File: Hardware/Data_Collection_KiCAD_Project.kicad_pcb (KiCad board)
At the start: 4 copper layers, 80 x 93.3 mm, 78 parts, among them J1 L717SDC37P1ACH4F, J2 Conn_Coaxial, J3 10118192-0001LF, Q1 SI1040X-T1-GE3, SW1 MCU Reset, U1 BNO055, U2 W25Q32JVSS, U3 MAX-8Q, U4 LP38692MPX-ADJ, U5 USBLC6-2SC6, U6 MCP9808_MSOP, U7 MS5607-02BA, U8 KX134-1211, U9 STM32L562VET6Q, Y1 32.768kHz, Y2 32MHz

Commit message: wtf is wrong with my github install
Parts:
- removed the G*** at (102.6, 98.5)
- JP1: footprint Jumper:SolderJumper-2_P1.3mm_Bridged_Pad1.0x1.5mm -> Jumper:SolderJumper-2_P1.3mm_Open_Pad1.0x1.5mm
- moved C30 69.1 mm to (130.7, 84.2), turned to 45 degrees
- moved U8 65.9 mm to (102.0, 133.0)
- moved C13 65.9 mm to (100.0, 135.9)
- moved C28 65.9 mm to (104.0, 135.9)
- moved U2 63.3 mm to (130.5, 90.2), turned to 45 degrees
- moved C27 60.1 mm to (104.4, 119.2)
- moved C1 60.1 mm to (104.2, 122.9)
- moved U1 60.1 mm to (109.1, 122.3)
- moved Y1 60.1 mm to (108.0, 116.3)
- moved C3 60.1 mm to (109.7, 113.5)
- moved C4 60.1 mm to (106.3, 113.5)
- moved C12 40.0 mm to (129.4, 101.5)
- moved U7 40.0 mm to (129.4, 105.1)
- moved C8 19.2 mm to (144.1, 104.9), turned to 90 degrees
- moved C7 19.1 mm to (142.6, 104.9), turned to 90 degrees
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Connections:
- D2 pad 2: Net-(D2-Pad2) -> unconnected-(D2-Pad2)
- D3 pad 2: Net-(D3-Pad2) -> unconnected-(D3-Pad2)
- D4 pad 2: Net-(D4-Pad2) -> unconnected-(D4-Pad2)
- D5 pad 2: Net-(D5-Pad2) -> unconnected-(D5-Pad2)
- D6 pad 2: Net-(D6-Pad2) -> unconnected-(D6-Pad2)
- U4 pad 1: GND -> +5V
- U4 pad 2: +5V -> Net-(R4-Pad1)
- U4 pad 3: +5V -> +3V3
- U4 pad 4: Net-(R4-Pad1) -> +5V
- U4 pad 5: +3V3 -> GND
- U9 pad 29: /FLASH_CLK -> /TELEMETRY_SCK
- U9 pad 30: /FLASH_MISO -> /TELEMETRY_MISO
- U9 pad 31: /FLASH_MOSI -> /TELEMETRY_MOSI
- U9 pad 35: Net-(D2-Pad2) -> unconnected-(U9-Pad35)
- U9 pad 36: Net-(D3-Pad2) -> unconnected-(U9-Pad36)
- U9 pad 37: Net-(D4-Pad2) -> /ABORT_1
- U9 pad 38: Net-(D5-Pad2) -> /ABORT_2
- U9 pad 39: Net-(D6-Pad2) -> unconnected-(U9-Pad39)
- U9 pad 52: /TELEMETRY_SCK -> /FLASH_CLK
- U9 pad 53: /TELEMETRY_MISO -> /FLASH_MISO
- U9 pad 54: /TELEMETRY_MOSI -> /FLASH_MOSI
- U9 pad 61: /ABORT_2 -> unconnected-(U9-Pad61)
- U9 pad 62: /ABORT_1 -> unconnected-(U9-Pad62)
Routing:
- net /SWCLK: track 0.00 -> 48.6 mm, vias 0 -> 2
- net /SWDIO: track 0.00 -> 42.5 mm, vias 0 -> 1
- net /GPS_TX: track 0.00 -> 39.9 mm, vias 0 -> 2
- net /GPS_RX: track 0.00 -> 38.7 mm
- net /~{GPS_RESET}: track 0.00 -> 35.6 mm
- net /ABORT_2: track 0.00 -> 32.3 mm, vias 0 -> 1
- net /ALERT_SDA: track 0.00 -> 31.5 mm
- net /ALERT_SCL: track 0.00 -> 30.2 mm
- net /ALERT_EN: track 0.00 -> 29.1 mm, vias 0 -> 1
- net /TELEMETRY_MOSI: track 0.00 -> 29.0 mm, vias 0 -> 2
- net /ABORT_1: track 0.00 -> 29.0 mm, vias 0 -> 1
- net /TELEMETRY_SCK: track 0.00 -> 27.2 mm, vias 0 -> 2
- net /TELEMETRY_MISO: track 0.00 -> 23.0 mm
- net /SENSOR_SCL: track 0.00 -> 20.9 mm
- net /SENSOR_SDA: track 0.00 -> 20.3 mm
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
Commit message: almost there
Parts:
- moved C2 106.7 mm to (112.3, 117.8)
- moved TP1 93.8 mm to (111.1, 121.2)
- moved TP3 89.8 mm to (122.7, 128.7)
- moved TP2 89.5 mm to (117.5, 110.3)
- moved C29 63.7 mm to (106.1, 131.4), turned to 180 degrees
- moved U6 57.6 mm to (108.2, 135.4), turned to 90 degrees
- moved R12 57.1 mm to (135.8, 95.5), turned to 180 degrees
- moved R11 53.9 mm to (139.3, 95.5)
- moved D6 47.3 mm to (154.0, 99.8), turned to -90 degrees
- moved R10 46.6 mm to (152.1, 99.7), turned to 90 degrees
- moved D4 44.4 mm to (154.0, 91.2), turned to -90 degrees
- moved C33 44.1 mm to (175.2, 114.0)
- moved R7 43.8 mm to (152.1, 87.0), turned to 90 degrees
- moved R9 39.7 mm to (152.1, 95.5), turned to 90 degrees
- moved D5 39.7 mm to (154.0, 95.5), turned to -90 degrees
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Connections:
- D2 pad 1: Net-(D2-Pad1) -> GND
- D2 pad 2: unconnected-(D2-Pad2) -> Net-(D2-Pad2)
- D3 pad 1: Net-(D3-Pad1) -> GND
- D3 pad 2: unconnected-(D3-Pad2) -> Net-(D3-Pad2)
- D4 pad 1: Net-(D4-Pad1) -> GND
- D4 pad 2: unconnected-(D4-Pad2) -> Net-(D4-Pad2)
- D5 pad 1: Net-(D5-Pad1) -> GND
- D5 pad 2: unconnected-(D5-Pad2) -> Net-(D5-Pad2)
- D6 pad 1: Net-(D6-Pad1) -> GND
- D6 pad 2: unconnected-(D6-Pad2) -> Net-(D6-Pad2)
- R10 pad 1: GND -> Net-(D6-Pad2)
- R10 pad 2: Net-(D6-Pad1) -> unconnected-(R10-Pad2)
- R6 pad 1: GND -> Net-(D2-Pad2)
- R6 pad 2: Net-(D2-Pad1) -> unconnected-(R6-Pad2)
- R7 pad 1: GND -> Net-(D3-Pad2)
- R7 pad 2: Net-(D3-Pad1) -> unconnected-(R7-Pad2)
- R8 pad 1: GND -> Net-(D4-Pad2)
- R8 pad 2: Net-(D4-Pad1) -> unconnected-(R8-Pad2)
- R9 pad 1: GND -> Net-(D5-Pad2)
- R9 pad 2: Net-(D5-Pad1) -> unconnected-(R9-Pad2)
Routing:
- net /SENSOR_SCL: track 20.9 -> 126.4 mm, vias 0 -> 6
- net /SENSOR_SDA: track 20.3 -> 114.4 mm
- net (no net): track 10.6 -> 0.00 mm, vias 6 -> 1
- net /BNO055/~{BNO055_BTL}: track 0.00 -> 6.62 mm
- net /KX134-1211/KX134_INT1: track 0.00 -> 5.42 mm
- net /BNO055/~{BNO055_RESET}: track 0.00 -> 4.76 mm
- net +3V3: track 90.2 -> 92.8 mm, vias 24 -> 26
- net /~{GPS_RESET}: track 35.6 -> 37.8 mm
- net Net-(D2-Pad2): track 0.00 -> 1.98 mm
- net Net-(D3-Pad2): track 0.00 -> 1.96 mm
- net Net-(D4-Pad2): track 0.00 -> 1.94 mm
- net Net-(D6-Pad2): track 0.00 -> 1.92 mm
- net Net-(D5-Pad2): track 0.00 -> 1.91 mm
- net GND: track 132.6 -> 134.4 mm, vias 70 -> 71
- net Net-(C2-Pad2): track 0.00 -> 1.62 mm

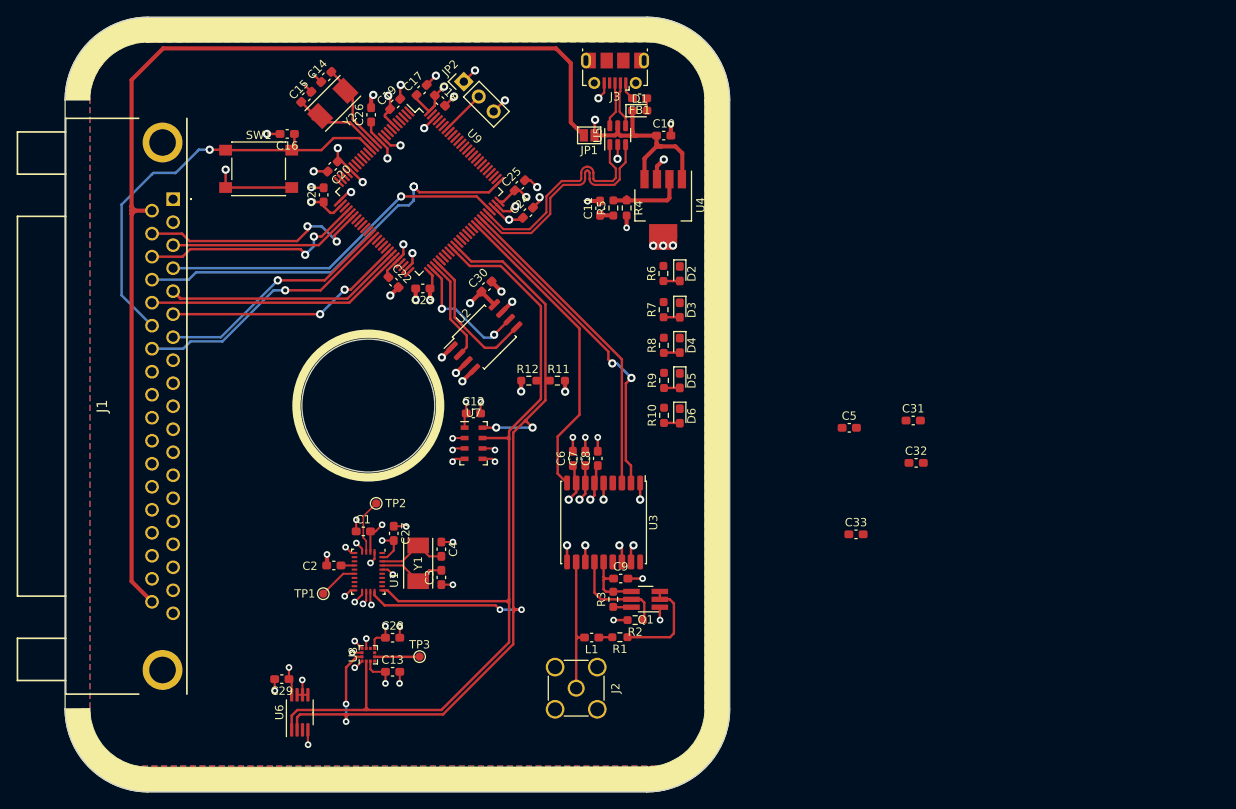
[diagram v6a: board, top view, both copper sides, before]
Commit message: Replaced Temp Sense and finalized routing
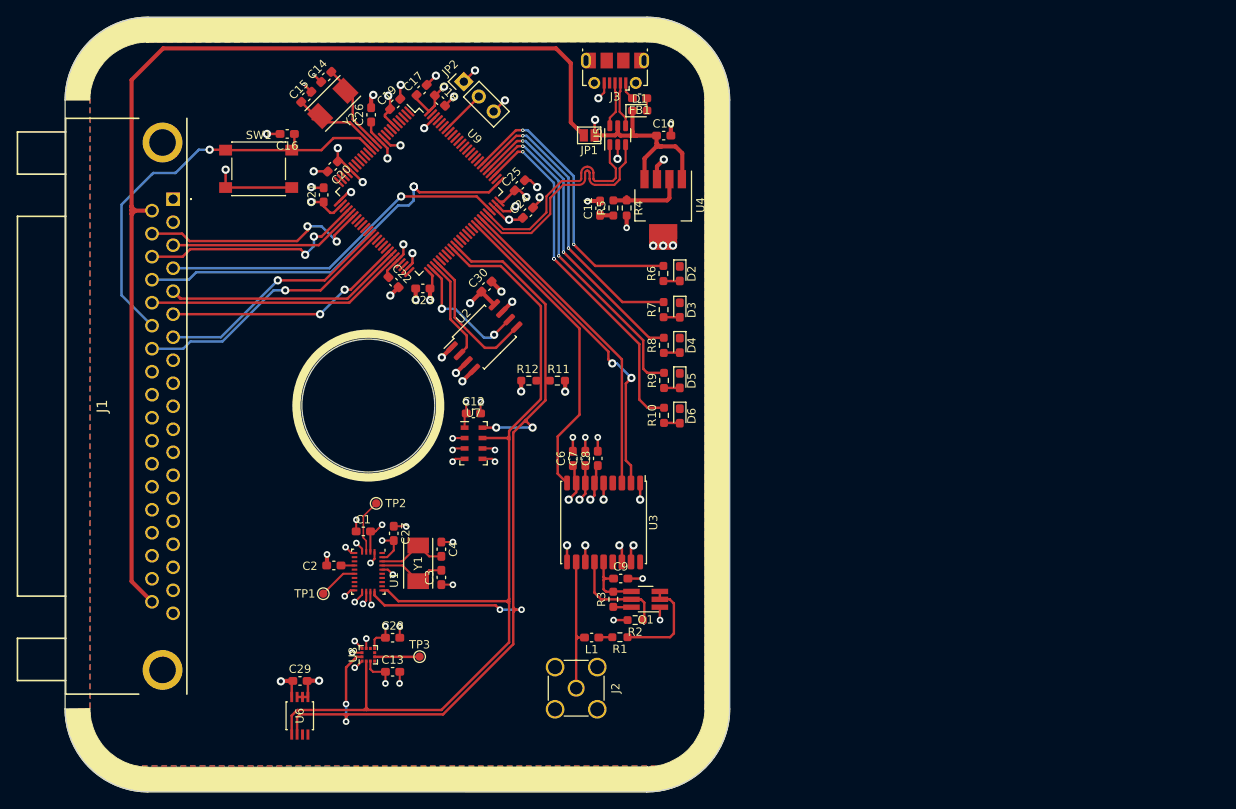
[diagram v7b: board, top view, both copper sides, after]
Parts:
- removed C31, C32, C33: 0.1uF, Capacitor_SMD:C_0603_1608Metric_Pad1.08x0.95mm_HandSolder
- removed C5: 1uF, Capacitor_SMD:C_0603_1608Metric_Pad1.08x0.95mm_HandSolder
- U6: value MCP9808_MSOP -> MIC184YMM-TR; footprint Package_SO:MSOP-8_3x3mm_P0.65mm -> RDT_Custom_Footprints:MIC184YMM-TR
- moved C29 2.20 mm to (108.3, 131.7), turned to 0 degrees
- moved U6 0.41 mm to (108.3, 135.8)
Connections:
- net /MCP9808/ALERT renamed /MIC184YYM/ALERT
- R10 pad 2: unconnected-(R10-Pad2) -> Net-(R10-Pad2)
- R6 pad 2: unconnected-(R6-Pad2) -> Net-(R6-Pad2)
- R7 pad 2: unconnected-(R7-Pad2) -> Net-(R7-Pad2)
- R8 pad 2: unconnected-(R8-Pad2) -> Net-(R8-Pad2)
- R9 pad 2: unconnected-(R9-Pad2) -> Net-(R9-Pad2)
- U9 pad 78: /MCU STM32L562VET6Q/SPI3_SCK -> Net-(R10-Pad2)
- U9 pad 79: /MCU STM32L562VET6Q/SPI3_MISO -> Net-(R9-Pad2)
- U9 pad 80: /MCU STM32L562VET6Q/SPI3_MOSI -> Net-(R8-Pad2)
- U9 pad 81: /MCU STM32L562VET6Q/~{SPI2_NSS} -> Net-(R7-Pad2)
- U9 pad 82: /MCU STM32L562VET6Q/SPI3_EXT_INT -> Net-(R6-Pad2)
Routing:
- net Net-(R10-Pad2): track 0.00 -> 43.8 mm, vias 0 -> 3
- net Net-(R9-Pad2): track 0.00 -> 40.8 mm, vias 0 -> 2
- net Net-(R8-Pad2): track 0.00 -> 37.6 mm, vias 0 -> 2
- net Net-(R7-Pad2): track 0.00 -> 36.4 mm, vias 0 -> 2
- net Net-(R6-Pad2): track 0.00 -> 35.1 mm, vias 0 -> 2
- net GND: track 134.4 -> 132.9 mm, vias 71 -> 69

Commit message: I think it is done....
maybe

hopefully

please
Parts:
- added G***: LOGO, XYZ:XYZ_Plane, F.Cu at (106.6, 109.2)
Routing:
- net GND: track 132.9 -> 136.7 mm, vias 69 -> 84
- net Net-(C15-Pad1): track 10.7 -> 10.1 mm
- net Net-(R10-Pad2): vias 3 -> 2
- net /ALERT_EN: vias 1 -> 2
- net (no net): vias 1 -> 0
